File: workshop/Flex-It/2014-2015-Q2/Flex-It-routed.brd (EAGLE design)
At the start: 84 x 80 mm, 14 parts, among them IC1 NE555D, Q1 MMBT2222A

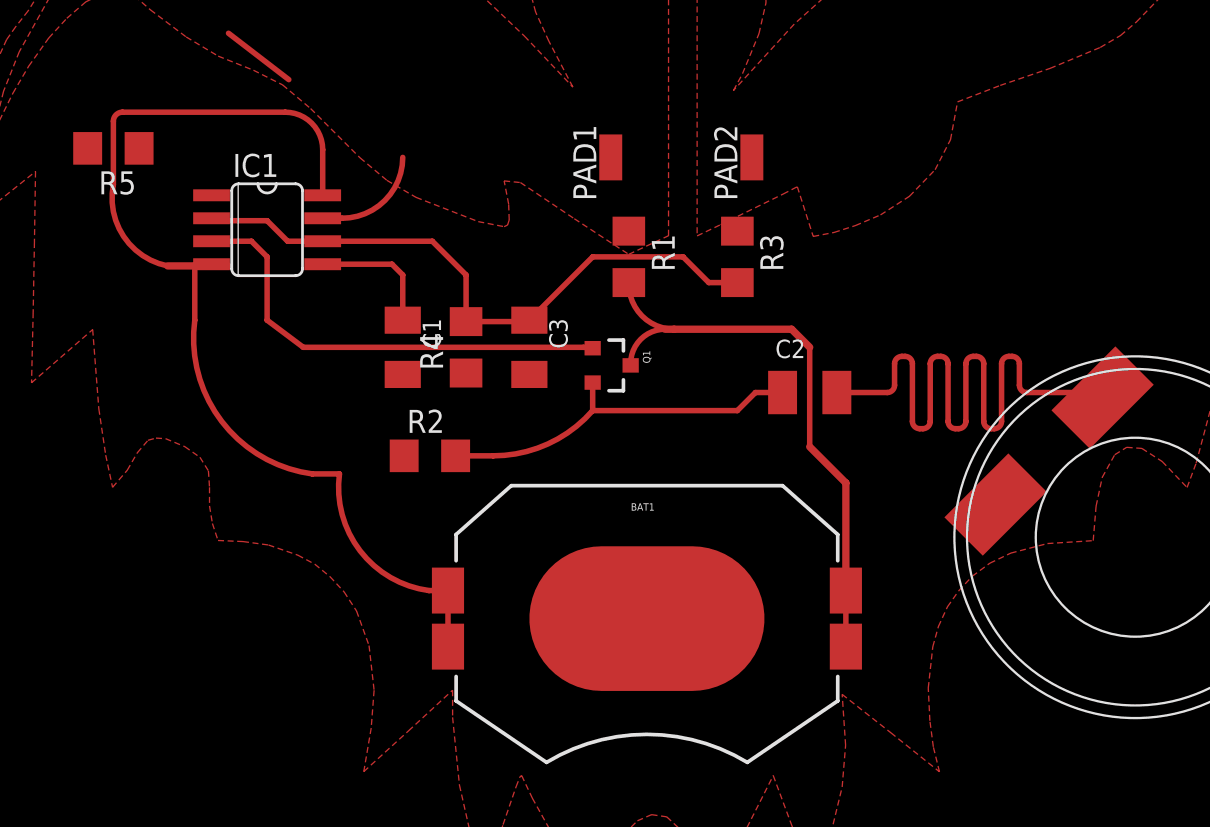
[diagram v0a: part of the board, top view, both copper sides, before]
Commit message: Thicker traces
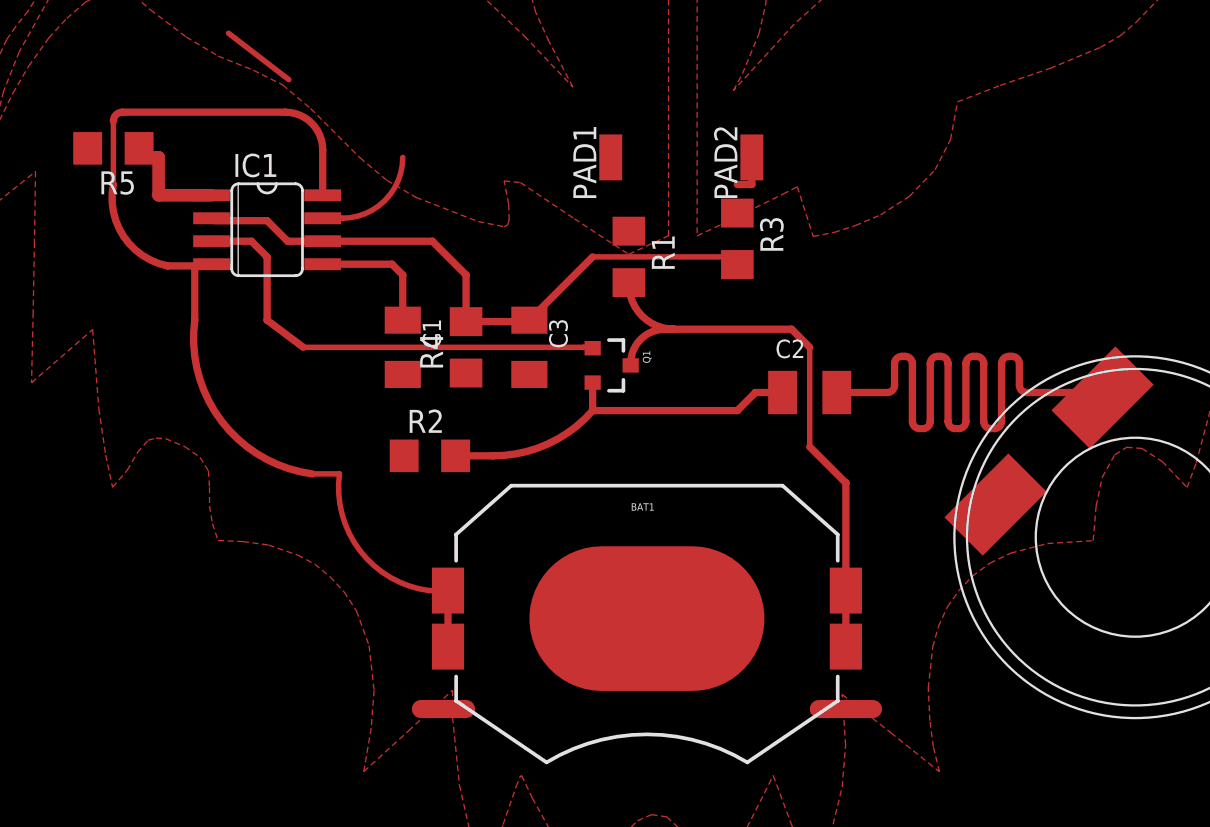
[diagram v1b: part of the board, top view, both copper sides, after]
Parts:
- moved R3 1.00 mm to (47.0, 37.0)
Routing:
- net GND: track 0.00 -> 12.1 mm
- net TOUCH2: track 0.00 -> 2.30 mm
